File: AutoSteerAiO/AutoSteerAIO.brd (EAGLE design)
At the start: 114.3 x 108 mm, 88 parts, among them K4 CB1A-P-12V, U1 VX7805-1000

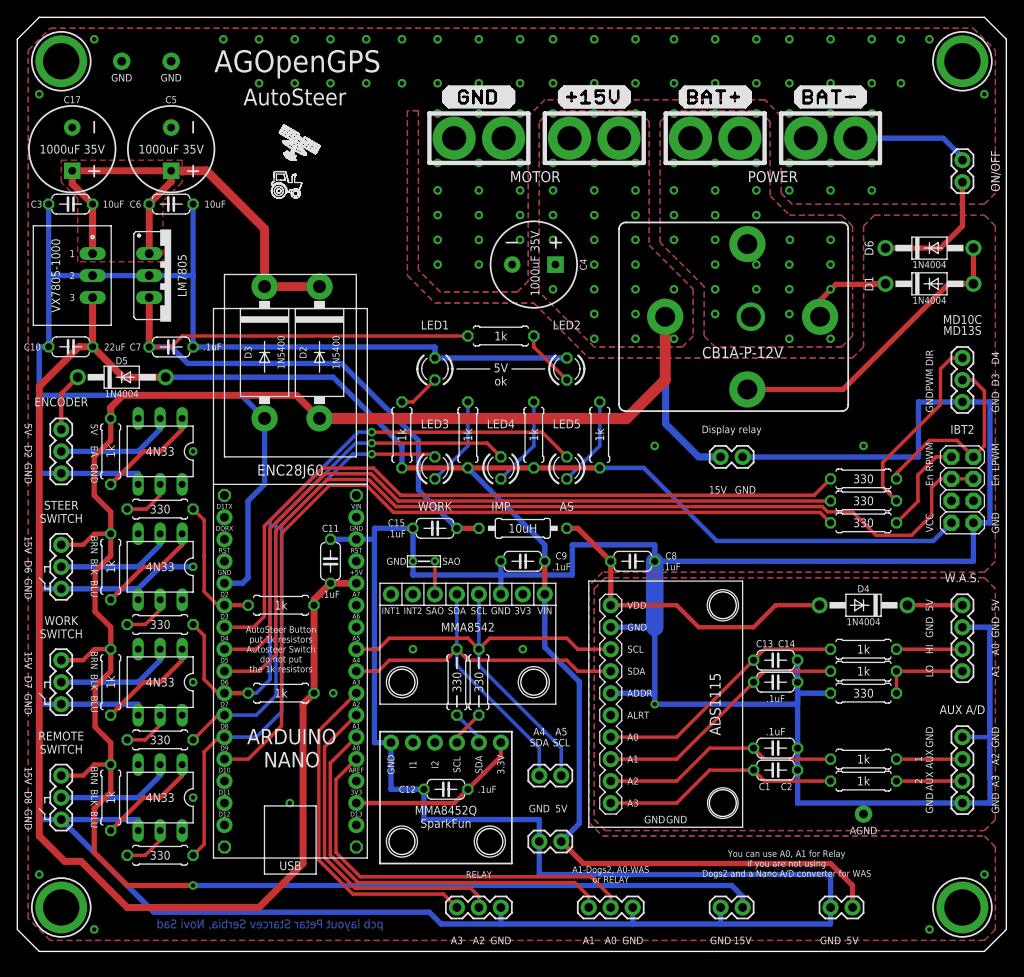
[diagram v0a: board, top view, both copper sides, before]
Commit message: Added selector for En IBT2, you can also use the new AutosteerPCBv2.ino sketch
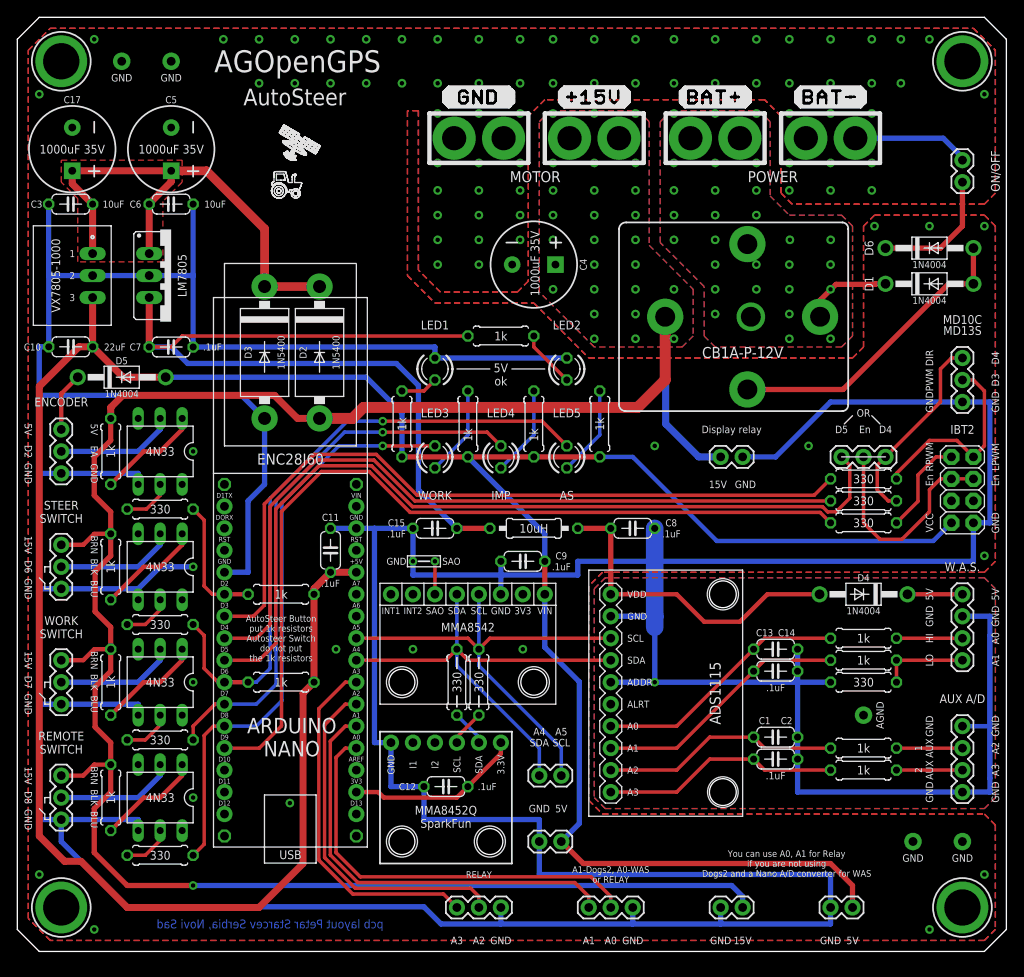
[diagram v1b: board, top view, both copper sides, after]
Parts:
- added OR: CONNECTOR 1x3 PINS, SparkFun-Connectors:1X03
- moved C8 3.81 mm to (71.1, 48.9)
- moved C1 1.27 mm to (87.6, 22.2)
- moved PCB1 1.27 mm to (31.6, 33.7)
- moved R10 1.27 mm to (97.8, 33.7)
- moved R11 1.27 mm to (97.8, 36.2)
- moved R17 1.27 mm to (44.5, 61.0)
- moved R21 1.27 mm to (67.3, 61.0)
- moved R6 1.27 mm to (52.1, 61.0)
- moved R7 1.27 mm to (59.7, 61.0)
- moved ADS1115 1.27 mm to (74.9, 29.8)
- moved AUX_A/D 1.27 mm to (109.2, 18.4)
- moved C13 1.27 mm to (87.6, 32.4)
- moved C2 1.27 mm to (87.6, 24.8)
- moved R14 1.27 mm to (97.8, 23.5)
- moved R15 1.27 mm to (30.5, 31.1)
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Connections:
- new net EN: IBT2.3, IBT2.4, OR.2
- net D5: now also OR.1; no longer IBT2.3, IBT2.4
- net DIR: now also OR.3
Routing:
- net EN: track 0.00 -> 25.5 mm
- net D5: track 111.3 -> 98.7 mm
- net GND: track 743.4 -> 736.5 mm, vias 90 -> 96
- net N$25: track 93.2 -> 98.2 mm
- net +5V: track 337.0 -> 341.0 mm
- net D9: track 98.0 -> 100.3 mm
- net D7: track 62.1 -> 64.3 mm
- net D8: track 66.2 -> 68.3 mm
- net A2: track 38.9 -> 41.0 mm
- net A0: track 46.9 -> 48.9 mm
- net A1: track 48.0 -> 50.0 mm
- net A3: track 39.3 -> 41.3 mm
- net D4: track 87.0 -> 88.5 mm
- net D3: track 85.9 -> 87.4 mm
- net DIR: track 21.7 -> 22.8 mm
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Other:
- board text added: "D5"

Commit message: Added one more 15V connector
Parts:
- added 15V2: CONNECTOR 1x2 PINS, SparkFun-Connectors:1X02
- moved 15V1 6.84 mm to (77.5, 54.6), turned to 90 degrees
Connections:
- net +15V: now also 15V2.2
- net GND: now also 15V2.1
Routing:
- net GND: track 736.5 -> 743.9 mm
- net +15V: track 249.1 -> 256.1 mm
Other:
- board text added: "Power"
- board text removed: "Display relay"
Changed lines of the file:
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@@
 <wire x1="50.8" y1="28.2575" x2="50.8" y2="29.5275" width="0.2032" layer="21"/>
 <wire x1="53.34" y1="28.2575" x2="53.34" y2="29.5275" width="0.2032" layer="21"/>
-<text x="80.9625" y="53.975" size="0.8636" layer="25" font="vector" ratio="15" rot="SR0" align="center">15V</text>
-<text x="84.1375" y="53.975" size="0.8636" layer="25" font="vector" ratio="15" rot="SR0" align="center">GND</text>
-<text x="82.55" y="60.325" size="0.8636" layer="25" font="vector" ratio="15" rot="SR0" align="center">Display relay</text>
+<text x="82.55" y="57.15" size="0.8636" layer="25" font="vector" ratio="15" rot="SR90" align="center">15V</text>
+<text x="82.55" y="54.61" size="0.8636" layer="25" font="vector" ratio="15" rot="SR90" align="center">GND</text>
+<text x="82.55" y="60.325" size="0.8636" layer="25" font="vector" ratio="15" rot="SR0" align="center">Power</text>
 <wire x1="52.07" y1="27.6225" x2="52.07" y2="26.9875" width="0.8128" layer="22"/>
 <wire x1="52.07" y1="35.2425" x2="52.07" y2="34.6075" width="0.8128" layer="22"/>
@@
 <wire x1="99.06" y1="57.4675" x2="99.06" y2="56.8325" width="0.8128" layer="22"/>
 <wire x1="96.52" y1="57.4675" x2="96.52" y2="56.8325" width="0.8128" layer="22"/>
+<wire x1="87.3125" y1="55.88" x2="87.9475" y2="55.88" width="0.8128" layer="22"/>
+<wire x1="77.1525" y1="55.88" x2="77.7875" y2="55.88" width="0.8128" layer="22"/>
 </plain>
 <attributes>
@@
 <attribute name="VALUE" x="53.34" y="31.115" size="1.016" layer="25" font="vector" ratio="12" rot="R270" align="center"/>
 </element>
-<element name="15V1" library="SparkFun-Connectors" library_urn="urn:adsk.eagle:library:513" package="1X02" package3d_urn="urn:adsk.eagle:package:38039/1" value="CONNECTOR 1x2 PINS" x="83.82" y="57.15" smashed="yes" rot="R180">
-<attribute name="MF" value="" x="83.82" y="57.15" size="1.778" layer="27" rot="R180" display="off"/>
-<attribute name="MPN" value="" x="83.82" y="57.15" size="1.778" layer="27" rot="R180" display="off"/>
-<attribute name="OC_NEWARK" value="unknown" x="83.82" y="57.15" size="1.778" layer="27" rot="R180" display="off"/>
+<element name="15V1" library="SparkFun-Connectors" library_urn="urn:adsk.eagle:library:513" package="1X02" package3d_urn="urn:adsk.eagle:package:38039/1" value="CONNECTOR 1x2 PINS" x="77.47" y="54.61" smashed="yes" rot="R90">
+<attribute name="MF" value="" x="77.47" y="54.61" size="1.778" layer="27" rot="R90" display="off"/>
+<attribute name="MPN" value="" x="77.47" y="54.61" size="1.778" layer="27" rot="R90" display="off"/>
+<attribute name="OC_NEWARK" value="unknown" x="77.47" y="54.61" size="1.778" layer="27" rot="R90" display="off"/>
 </element>
 <element name="U$13" library="#MMA8542Q" package="MMA8542Q" value="MMA8542Q" x="57.15" y="10.16" smashed="yes" rot="R90"/>
@@
 <attribute name="NAME" x="97.79" y="62.23" size="0.8636" layer="25" font="vector" ratio="15" rot="SR0" align="center"/>
 <attribute name="OC_NEWARK" value="unknown" x="95.25" y="57.15" size="1.778" layer="27" display="off"/>
+</element>
+<element name="15V2" library="SparkFun-Connectors" library_urn="urn:adsk.eagle:library:513" package="1X02" package3d_urn="urn:adsk.eagle:package:38039/1" value="CONNECTOR 1x2 PINS" x="87.63" y="54.61" smashed="yes" rot="R90">
+<attribute name="MF" value="" x="87.63" y="54.61" size="1.778" layer="27" rot="R90" display="off"/>
+<attribute name="MPN" value="" x="87.63" y="54.61" size="1.778" layer="27" rot="R90" display="off"/>
+<attribute name="OC_NEWARK" value="unknown" x="87.63" y="54.61" size="1.778" layer="27" rot="R90" display="off"/>
 </element>
 </elements>
@@
 <contactref element="R6" pad="1"/>
 <wire x1="107.95" y1="49.53" x2="105.8545" y2="47.4345" width="0.508" layer="16"/>
-<wire x1="105.8545" y1="47.4345" x2="80.8355" y2="47.4345" width="0.508" layer="16"/>
-<wire x1="80.8355" y1="47.4345" x2="71.12" y2="57.15" width="0.508" layer="16"/>
-<wire x1="67.31" y1="57.15" x2="71.12" y2="57.15" width="0.508" layer="16"/>
+<wire x1="105.8545" y1="47.4345" x2="79.5655" y2="47.4345" width="0.508" layer="16"/>
+<wire x1="79.5655" y1="47.4345" x2="69.85" y2="57.15" width="0.508" layer="16"/>
+<wire x1="67.31" y1="57.15" x2="69.85" y2="57.15" width="0.508" layer="16"/>
 <wire x1="52.07" y1="57.15" x2="44.45" y2="57.15" width="0.6096" layer="1"/>
 <wire x1="59.69" y1="57.15" x2="52.07" y2="57.15" width="0.6096" layer="1"/>
@@
 <wire x1="46.99" y1="15.24" x2="60.325" y2="15.24" width="0.6096" layer="16"/>
 <wire x1="60.325" y1="15.24" x2="60.325" y2="12.7" width="0.6096" layer="16"/>
-<wire x1="109.22" y1="63.5" x2="93.98" y2="63.5" width="0.6096" layer="16"/>
-<wire x1="93.98" y1="63.5" x2="87.63" y2="57.15" width="0.6096" layer="16"/>
-<wire x1="83.82" y1="57.15" x2="87.63" y2="57.15" width="0.6096" layer="16"/>
+<wire x1="109.22" y1="63.5" x2="98.425" y2="63.5" width="0.6096" layer="16"/>
+<wire x1="98.425" y1="63.5" x2="89.535" y2="54.61" width="0.6096" layer="16"/>
+<wire x1="77.47" y1="54.61" x2="89.535" y2="54.61" width="0.6096" layer="16"/>
 <wire x1="46.9769125" y1="5.1646625" x2="12.6153375" y2="5.1646625" width="0.6096" layer="16"/>
 <wire x1="12.6153375" y1="5.1646625" x2="5.08" y2="12.7" width="0.6096" layer="16"/>
@@
 <via x="111.76" y="83.82" extent="1-16" drill="0.508"/>
 <via x="111.76" y="45.72" extent="1-16" drill="0.508"/>
+<contactref element="15V2" pad="1"/>
 </signal>
 <signal name="D5">
@@
 <via x="71.4375" y="87.9475" extent="1-16" drill="0.508"/>
 <contactref element="15V1" pad="2"/>
-<wire x1="74.87" y1="73.3425" x2="74.93" y2="73.2825" width="0.8128" layer="16"/>
-<wire x1="74.93" y1="73.2825" x2="74.93" y2="60.96" width="0.8128" layer="16"/>
-<wire x1="78.74" y1="57.15" x2="81.28" y2="57.15" width="0.8128" layer="16"/>
-<wire x1="78.74" y1="57.15" x2="74.93" y2="60.96" width="0.8128" layer="16"/>
+<contactref element="15V2" pad="2"/>
+<wire x1="74.87" y1="73.3425" x2="74.93" y2="73.2825" width="1.016" layer="16"/>
+<wire x1="74.93" y1="73.2825" x2="74.93" y2="59.69" width="1.016" layer="16"/>
+<wire x1="74.93" y1="59.69" x2="77.47" y2="57.15" width="1.016" layer="16"/>
+<wire x1="77.47" y1="57.15" x2="87.63" y2="57.15" width="1.016" layer="16"/>
 </signal>
 <signal name="HIGH">

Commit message: Add files via upload
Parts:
- added 5V2: CONNECTOR 1x2 PINS, SparkFun-Connectors:1X02
- moved 5V 3.81 mm to (97.8, 5.08), turned to 90 degrees
- moved 15V 1.27 mm to (82.5, 5.08), turned to 90 degrees
- moved C12 0.64 mm to (49.5, 18.4)
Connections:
- net +5V: now also 5V2.2
- net GND: now also 5V2.1
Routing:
- net GND: track 743.9 -> 708.3 mm, vias 96 -> 104
- net +15V: track 256.1 -> 253.1 mm
- net +3V3: track 20.3 -> 21.2 mm
- net N$26: track 59.2 -> 59.9 mm
- net +5V: track 341.0 -> 341.6 mm
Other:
- board text removed: "You can use A0, A1 for Relay if you are not using Dogs2 and a Nano A/D converter for WAS"

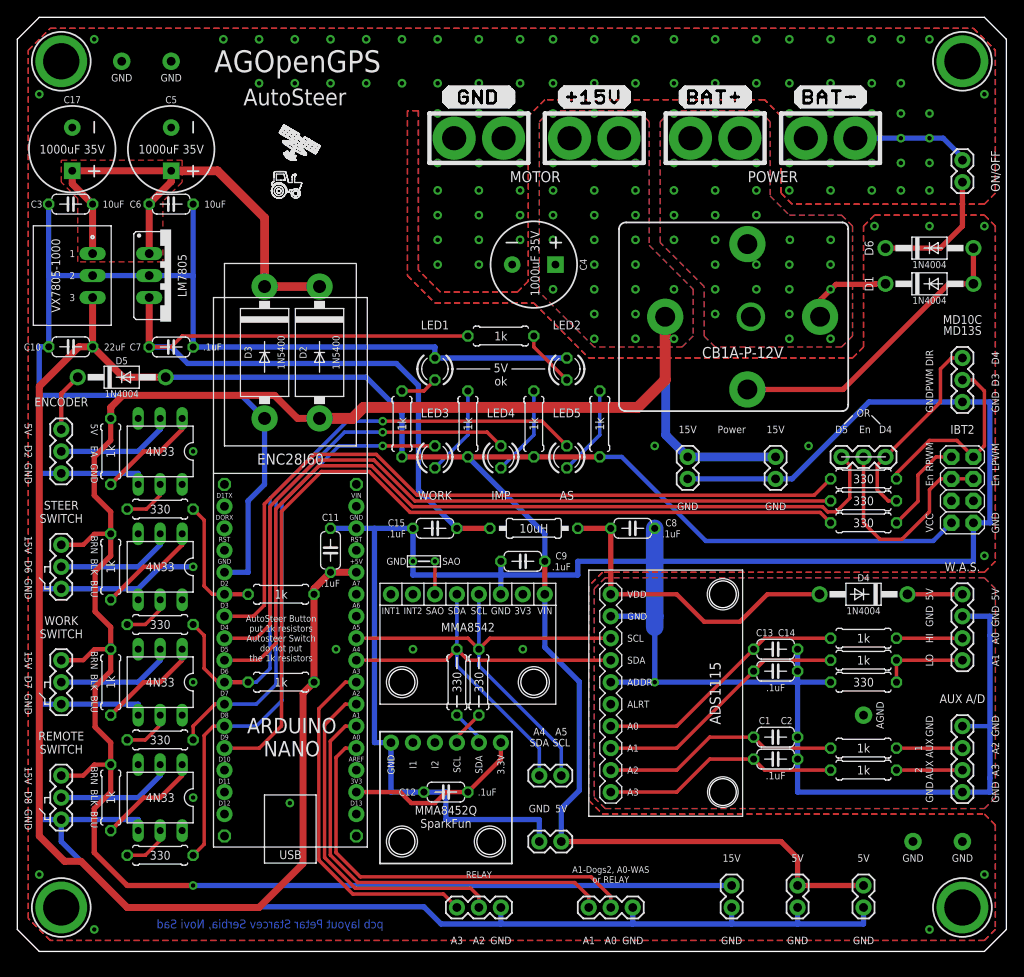
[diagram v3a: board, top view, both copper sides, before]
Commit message: Add files via upload
I removed the capacitors and the inductor has no need for them
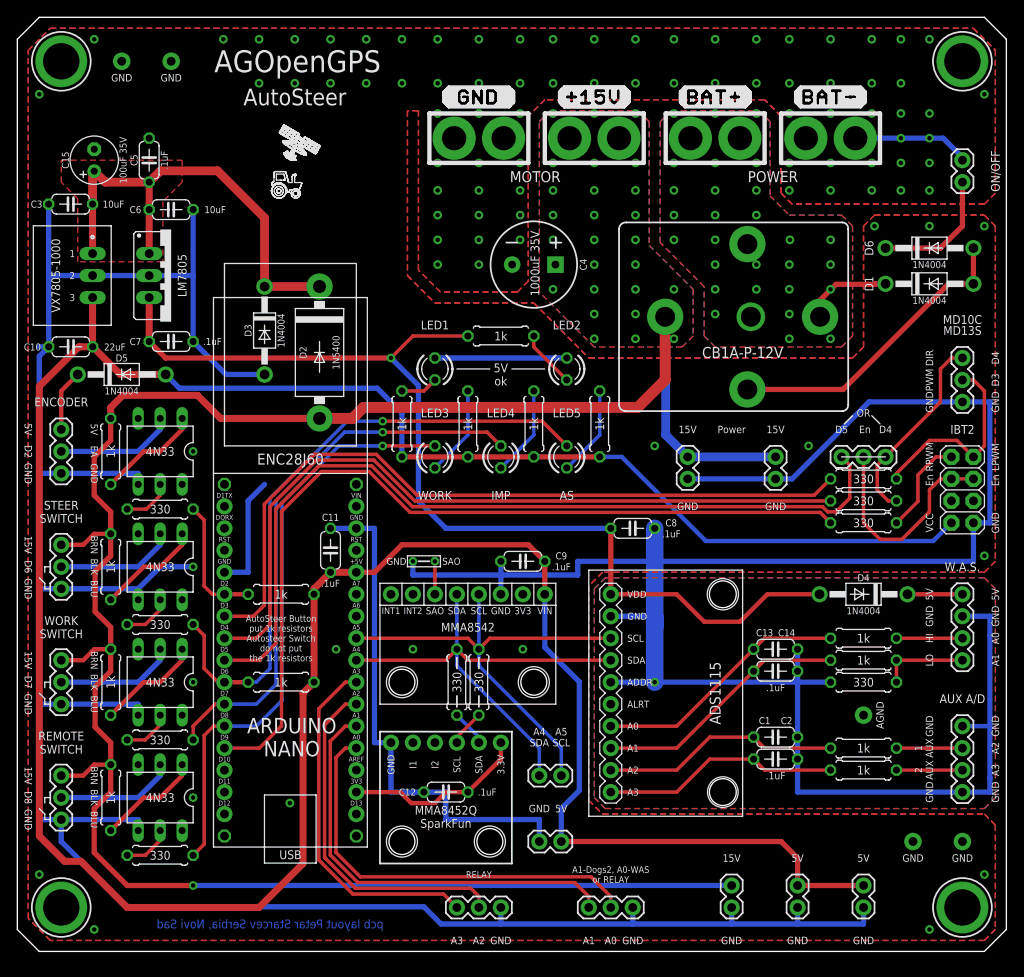
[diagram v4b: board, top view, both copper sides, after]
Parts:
- removed C17: 1000uF 35V, SparkFun-Capacitors:CPOL-RADIAL-5MM-10MM
- removed L1: 10uH, rcl:0207/10
- C15: value .1uF -> 100uF 35V; device resistor:C050-024X044 -> rcl:E2,5-6
- C5: value 1000uF 35V -> .1uF; device SparkFun-Capacitors:CPOL-RADIAL-5MM-10MM -> resistor:C050-024X044
- D3: value 1N5400 -> 1N4004; device #Diode 2:DO201-15 -> #adafruit:DO41-10
- moved C15 58.0 mm to (8.89, 91.4), turned to 90 degrees
- moved C5 2.84 mm to (15.2, 91.4)
- moved D3 2.54 mm to (28.6, 71.8)
- moved C6 0.64 mm to (17.8, 85.7)
- moved C7 0.64 mm to (17.8, 70.5)
- moved D5 0.32 mm to (12.1, 66.7)
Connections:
- removed net N$25: 7805.OUT, C15.2, C7.2, L1.1, R16.1
- net A+5V: now also 7805.OUT, C7.2, R16.1; no longer L1.2
- net GND: now also C15.-, C5.1; no longer C15.1, C17.-, C5.-
- net N$26: now also C15.+, C5.2; no longer C17.+, C5.+
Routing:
- net N$25: track 98.2 -> 0.00 mm
- net A+5V: track 38.2 -> 119.5 mm, vias 0 -> 1
- net GND: track 708.3 -> 652.7 mm
- net +5V: track 341.6 -> 349.7 mm
- net N$26: track 59.9 -> 55.8 mm

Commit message: Add files via upload
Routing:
- net N$26: track 55.8 -> 54.1 mm
- removed copper zone on layer 1, net N$26
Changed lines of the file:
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@@
 <wire x1="8.7" y1="86.3595" x2="8.7" y2="80.645" width="0.8128" layer="1"/>
 <wire x1="28.575" y1="76.835" x2="28.575" y2="84.7725" width="1.016" layer="1"/>
-<wire x1="28.575" y1="84.7725" x2="23.1375" y2="90.21" width="1.016" layer="1"/>
+<wire x1="28.575" y1="84.7725" x2="24.4075" y2="88.94" width="1.016" layer="1"/>
 <wire x1="15.24" y1="85.725" x2="15.24" y2="80.645" width="0.8128" layer="1"/>
 <contactref element="7805" pad="IN"/>
-<wire x1="15.24" y1="85.725" x2="15.24" y2="86.4" width="0.8128" layer="1"/>
-<polygon width="0.1524" layer="1" thermals="no">
-<vertex x="5.08" y="91.44"/>
-<vertex x="19.05" y="91.44"/>
-<vertex x="19.05" y="88.9"/>
-<vertex x="16.8275" y="86.6775"/>
-<vertex x="16.8275" y="79.6925"/>
-<vertex x="6.985" y="79.6925"/>
-<vertex x="6.985" y="86.995"/>
-<vertex x="5.08" y="88.9"/>
-</polygon>
 <wire x1="34.925" y1="76.835" x2="28.575" y2="76.835" width="1.016" layer="1"/>
 <contactref element="C5" pad="2"/>
 <contactref element="C15" pad="+"/>
-<wire x1="15.24" y1="88.9" x2="15.24" y2="85.725" width="0.8128" layer="1"/>
-<wire x1="23.1375" y1="90.21" x2="16.55" y2="90.21" width="1.016" layer="1"/>
+<wire x1="24.4075" y1="88.94" x2="15.28" y2="88.94" width="1.016" layer="1"/>
 <wire x1="8.6995" y1="86.36" x2="8.6995" y2="89.9795" width="1.016" layer="1"/>
 <wire x1="8.89" y1="90.17" x2="8.6995" y2="89.9795" width="1.016" layer="1"/>
-<wire x1="15.24" y1="88.9" x2="10.16" y2="88.9" width="1.016" layer="1"/>
-<wire x1="8.89" y1="90.17" x2="10.16" y2="88.9" width="1.016" layer="1"/>
-<wire x1="15.24" y1="88.9" x2="16.55" y2="90.21" width="1.016" layer="1"/>
+<wire x1="8.89" y1="90.17" x2="13.97" y2="90.17" width="1.016" layer="1"/>
+<wire x1="15.24" y1="88.9" x2="13.97" y2="90.17" width="1.016" layer="1"/>
+<wire x1="15.24" y1="88.9" x2="15.28" y2="88.94" width="1.016" layer="1"/>
+<wire x1="15.24" y1="88.9" x2="15.24" y2="85.725" width="0.8128" layer="1"/>
 </signal>
 <signal name="D2">

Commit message: Add files via upload
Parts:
- removed R4: 330, resistor:0207/7
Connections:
- net GND: no longer R4.2
- net LOW.: no longer R4.1
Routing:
- net GND: track 652.7 -> 648.9 mm
- net LOW.: track 10.2 -> 7.62 mm
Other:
- board text added: "REM"
- board text removed: "IMP"

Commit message: Add files via upload
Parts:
- removed OR: CONNECTOR 1x3 PINS, SparkFun-Connectors:1X03
- added 5V3: CONNECTOR 1x2 PINS, SparkFun-Connectors:1X02
- added J1: (no value), SparkFun-Connectors:1X01
- added U$1: MD13S, #Motor Drivers:MD13S
- added U$2: IBT2, #Motor Drivers:IBT2
- moved 1 17.2 mm to (48.9, 3.81)
- moved 0 9.61 mm to (41.3, 3.81)
- moved C9 5.99 mm to (53.3, 41.9)
- moved D4 5.68 mm to (92.7, 38.7)
- moved 5V 2.54 mm to (95.2, 5.08)
- moved 5V2 2.54 mm to (87.6, 5.08)
- moved C8 2.54 mm to (71.1, 46.4)
- moved MMA8542 2.54 mm to (41.9, 26.0)
- moved 15V 2.54 mm to (80.0, 5.08)
- moved R10 1.27 mm to (97.8, 32.4)
- moved R11 1.27 mm to (97.8, 34.9)
- moved C13 1.27 mm to (87.6, 31.1)
- moved 15V1 1.27 mm to (78.7, 54.6)
- moved C14 1.27 mm to (87.6, 33.7)
- moved K4 1.27 mm to (83.8, 74.6)
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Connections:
- removed net EN: IBT2.3, IBT2.4, OR.2
- removed net SAO: MMA8542.SAO
- new net A6: 0.2, PCB1.A6
- new net A7: 0.1, PCB1.A7
- net +5V: now also 5V3.2
- net A0: now also 1.3; no longer 1.2
- net A1: now also 1.2; no longer 1.1
- net A2: now also 1.1; no longer 0.2
- net A3: now also 0.3; no longer 0.1
- net D5: now also J1.1; no longer OR.1
- net DIR: now also IBT2.3, IBT2.4; no longer OR.3
- net GND: now also 5V3.1, MMA8542.SAO; no longer 0.3, 1.3
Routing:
- net GND: track 648.9 -> 490.0 mm, vias 104 -> 101
- net A7: track 0.00 -> 43.1 mm
- net A6: track 0.00 -> 42.1 mm
- net D5: track 98.7 -> 61.6 mm
- net EN: track 25.5 -> 0.00 mm
- net A0: track 48.9 -> 31.8 mm
- net A1: track 50.0 -> 32.9 mm
- net DIR: track 22.8 -> 38.5 mm
- net A+5V: track 119.5 -> 111.4 mm
- net A2: track 41.0 -> 34.1 mm
- net A3: track 41.3 -> 35.2 mm
- net A+5V.: track 6.35 -> 12.0 mm
- net SAO: track 3.81 -> 0.00 mm, vias 1 -> 0
- net SDA: track 55.4 -> 52.8 mm
- net V+: track 10.3 -> 8.98 mm
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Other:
- board text added: "A6"
- board text added: "A7"
- board text added: "or ENCODER"
- board text removed: "A1-Dogs2, A0-WAS or RELAY"
- board text removed: "AS"
- board text removed: "RELAY"
- board text removed: "REM"
- board text removed: "SAO"
- board text removed: "WORK"
